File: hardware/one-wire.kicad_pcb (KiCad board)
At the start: 2 copper layers, 30 x 30 mm, 27 parts, among them P1 CON-SENSOR2, P2 DEBUG, P3 BOOT, P4 CONN_02X03, P5 CONN_01X03, U1 XMC1100-16, U2 NC7WZ07, U3 DRILL, U4 DRILL, U5 DRILL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

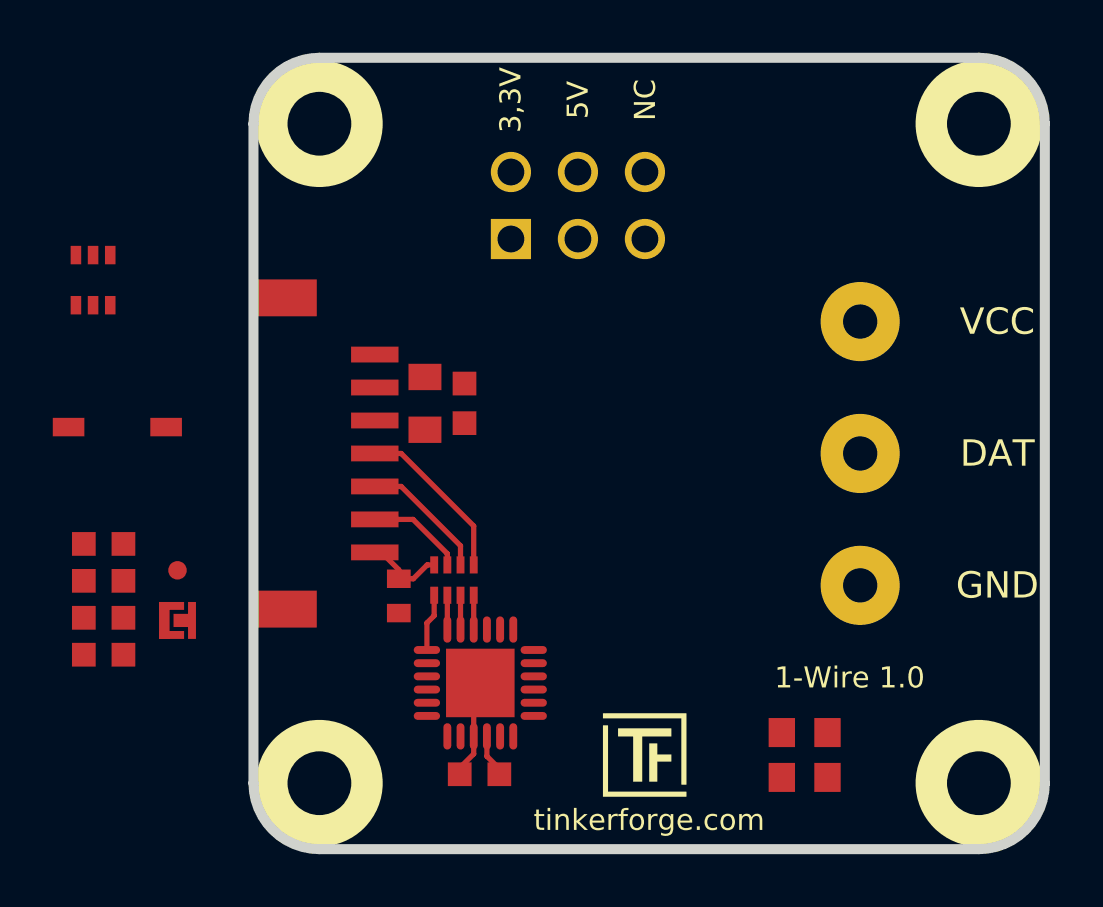
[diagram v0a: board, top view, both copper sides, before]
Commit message: one wire bricklet fully routed
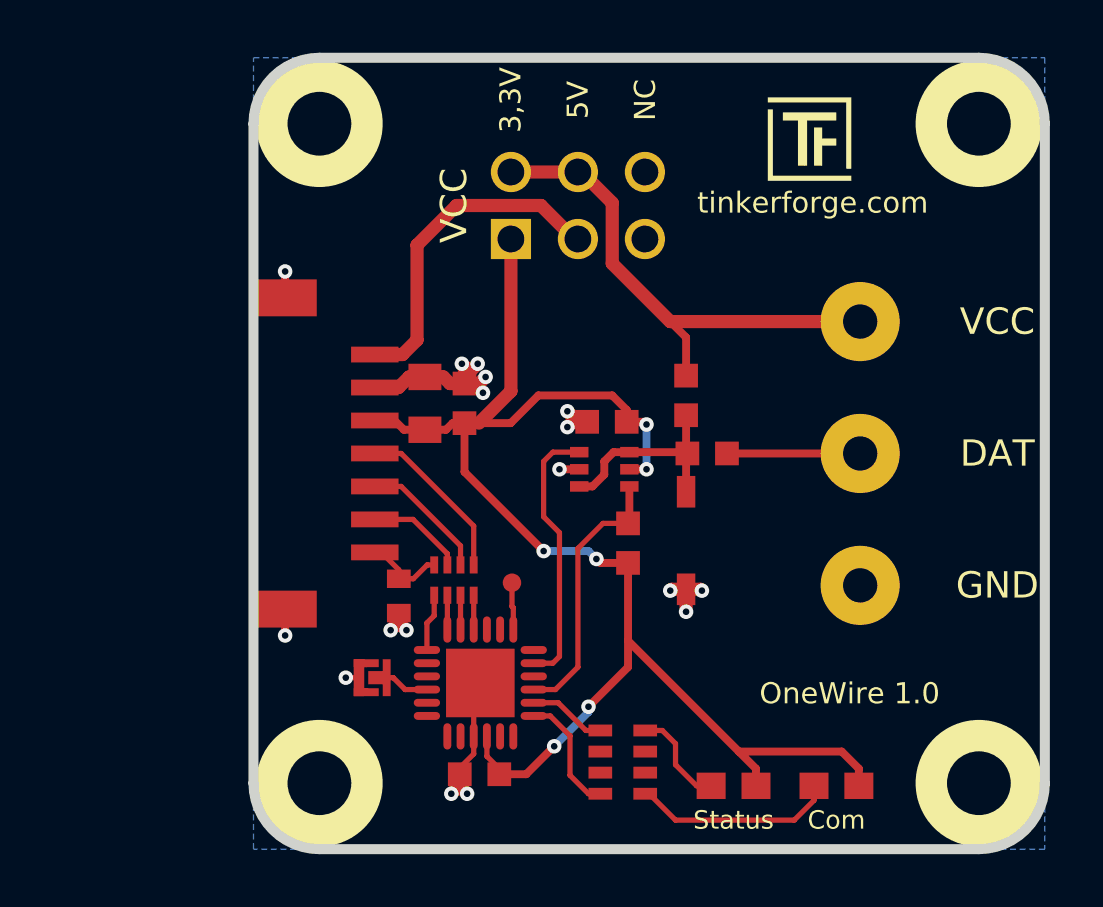
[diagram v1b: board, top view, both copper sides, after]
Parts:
- removed R4: 1k, R0603F
- added C5: 100nF, kicad-libraries:C0603F, F.Cu at (145.7, 123.5)
- added RP2: 1k, kicad-libraries:4X0603, F.Cu at (146.3, 136.4)
- C1: footprint C0805 -> kicad-libraries:C0805
- C2: footprint C0402E -> kicad-libraries:C0402E
- C3, C4: footprint C0603F -> kicad-libraries:C0603F
- D1, D3: footprint D0603E -> kicad-libraries:D0603E
- D2: footprint SOD-123 -> kicad-libraries:SOD-123
- P1: footprint CON-SENSOR2 -> kicad-libraries:CON-SENSOR2
- P4: footprint pin_array_3x2 -> kicad-libraries:pin_array_3x2
- R1: value 1k -> 100
- R2, R3: footprint R0603F -> kicad-libraries:R0603F
- RP1: footprint 4X0402 -> kicad-libraries:4X0402
- U3, U4, U5, U6: footprint DRILL_NP -> kicad-libraries:DRILL_NP
- moved G*** 31.7 mm to (147.3, 134.7), turned to 180 degrees
- moved G*** 24.3 mm to (147.3, 124.7), turned to 180 degrees
- moved G*** 24.2 mm to (151.8, 111.2)
- moved R2 23.2 mm to (148.7, 122.5), turned to 270 degrees
- moved R1 23.1 mm to (149.5, 124.7), turned to 180 degrees
- moved D2 22.0 mm to (148.7, 128.0), turned to 90 degrees
- moved U2 20.7 mm to (145.6, 125.3), turned to 270 degrees
- moved R3 20.1 mm to (146.5, 128.1), turned to 90 degrees
- moved VAL 18.7 mm to (139.3, 124.7), turned to 180 degrees
- moved P2 12.7 mm to (142.1, 129.6)
- moved P3 7.69 mm to (136.8, 133.2)
- moved D1 2.17 mm to (150.5, 137.3), turned to 180 degrees
- moved D3 1.22 mm to (154.4, 137.3), turned to 180 degrees
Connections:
- D2 pad 2: DAT -> Net-(D2-Pad2)
- P4 pad 5: Net-(P4-Pad5) -> (no net)
- P4 pad 6: Net-(P4-Pad6) -> (no net)
- R1 pad 1: Net-(R1-Pad1) -> DAT
- R1 pad 2: Net-(D1-Pad2) -> Net-(D2-Pad2)
- R2 pad 2: DAT -> Net-(D2-Pad2)
- U1 pad 11: Net-(U1-Pad11) -> (no net)
- U1 pad 12: Net-(U1-Pad12) -> (no net)
- U1 pad 16: Net-(U1-Pad16) -> (no net)
- U1 pad 18: Net-(U1-Pad18) -> (no net)
- U1 pad 2: Net-(U1-Pad2) -> (no net)
- U1 pad 20: Net-(U1-Pad20) -> (no net)
- U1 pad 21: Net-(U1-Pad21) -> (no net)
- U1 pad 3: Net-(U1-Pad3) -> (no net)
- U1 pad 5: Net-(U1-Pad5) -> (no net)
- U1 pad 6: Net-(U1-Pad6) -> (no net)
- U1 pad 7: Net-(R1-Pad1) -> (no net)
- U1 pad 8: Net-(R4-Pad1) -> (no net)
- U2 pad 3: DAT -> Net-(D2-Pad2)
- U2 pad 6: DAT -> Net-(D2-Pad2)
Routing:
- net 3V3: track 1.64 -> 56.3 mm, vias 0 -> 6
- net VCC: track 0.00 -> 19.2 mm
- net GND: track 8.38 -> 27.6 mm, vias 0 -> 17
- net +5V: track 0.00 -> 12.7 mm
- net RX: track 0.00 -> 10.2 mm
- net TX: track 0.00 -> 10.2 mm
- net Net-(D2-Pad2): track 0.00 -> 7.89 mm
- net Net-(D3-Pad2): track 0.00 -> 7.67 mm
- net DAT: track 0.00 -> 5.05 mm
- net Net-(RP2-Pad5): track 0.00 -> 4.62 mm
- net Net-(D1-Pad2): track 0.00 -> 3.84 mm
- net Net-(RP2-Pad8): track 0.00 -> 2.96 mm
- net Net-(P3-Pad2): track 0.00 -> 2.51 mm
- net Net-(P2-Pad1): track 0.00 -> 1.80 mm
- added copper zone on B.Cu, net GND
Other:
- board text added: "Com"
- board text added: "OneWire 1.0"
- board text added: "Status"
- board text removed: "1-Wire 1.0"
